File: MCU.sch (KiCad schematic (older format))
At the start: 34 parts, among them Q1 BSS138, SW1 SW_Push, U2 STM32F722RETx

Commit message: Changes made
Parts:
- removed Q1: BSS138, Package_TO_SOT_SMD:SOT-23, symbol Transistor_FET:BSS138
- removed R1: 10k, Resistor_SMD:R_0402_1005Metric, symbol Device:R_Small
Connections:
- net BUZ-_MCU: no longer names the net of U2.24 (PC4)
- net UART6_TX: no longer names the net of U2.37 (PC6)
- no-connect marks 17 -> 19
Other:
- moved on the sheet: C13, C14, FB2
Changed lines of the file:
@@
-$EndComp
-Wire Wire Line
-	5100 2250 5100 2200
-Wire Wire Line
-	5100 2200 5200 2200
-Wire Wire Line
-	5200 2200 5250 2200
-Connection ~ 5200 2200
-Wire Wire Line
-	5200 2150 5200 2200
-Wire Wire Line
-	5200 1900 5450 1900
-Wire Wire Line
-	5200 1900 5200 1950
-Connection ~ 5200 1900
-Wire Wire Line
-	5100 1900 5200 1900
-$Comp
-L Transistor_FET:BSS138 Q1
-U 1 1 6086323C
-P 5450 2100
-F 0 "Q1" V 5699 2100 50  0000 C CNN
-F 1 "BSS138" V 5790 2100 50  0000 C CNN
-F 2 "Package_TO_SOT_SMD:SOT-23" H 5650 2025 50  0001 L CIN
-F 3 "https://www.fairchildsemi.com/datasheets/BS/BSS138.pdf" H 5450 2100 50  0001 L CNN
-	1    5450 2100
-	0    1    1    0
-$EndComp
-$Comp
-L Device:R_Small R1
-U 1 1 60863243
-P 5200 2050
-F 0 "R1" H 5004 2050 50  0000 C CNN
-F 1 "10k" H 5000 1950 50  0000 C CNN
-F 2 "Resistor_SMD:R_0402_1005Metric" H 5200 2050 50  0001 C CNN
-F 3 "~" H 5200 2050 50  0001 C CNN
-	1    5200 2050
-	1    0    0    -1
-$EndComp
-$Comp
-L power:GND #PWR013
-U 1 1 60863249
-P 5100 2250
-F 0 "#PWR013" H 5100 2000 50  0001 C CNN
-F 1 "GND" H 5105 2077 50  0000 C CNN
-F 2 "" H 5100 2250 50  0001 C CNN
-F 3 "" H 5100 2250 50  0001 C CNN
-	1    5100 2250
-	1    0    0    -1
 $EndComp
 Wire Wire Line
@@
 L power:+3.3VA #PWR012
 U 1 1 608633F9
-P 6350 850
-F 0 "#PWR012" H 6350 700 50  0001 C CNN
-F 1 "+3.3VA" H 6365 1023 50  0000 C CNN
-F 2 "" H 6350 850 50  0001 C CNN
-F 3 "" H 6350 850 50  0001 C CNN
-	1    6350 850
+P 5350 1650
+F 0 "#PWR012" H 5350 1500 50  0001 C CNN
+F 1 "+3.3VA" H 5365 1823 50  0000 C CNN
+F 2 "" H 5350 1650 50  0001 C CNN
+F 3 "" H 5350 1650 50  0001 C CNN
+	1    5350 1650
 	1    0    0    -1
 $EndComp
@@
 L Device:C_Small C14
 U 1 1 60863403
-P 6350 950
-F 0 "C14" H 6442 996 50  0000 L CNN
-F 1 "10nF" H 6442 905 50  0000 L CNN
-F 2 "Capacitor_SMD:C_0402_1005Metric" H 6350 950 50  0001 C CNN
-F 3 "~" H 6350 950 50  0001 C CNN
-	1    6350 950
+P 5350 1750
+F 0 "C14" H 5442 1796 50  0000 L CNN
+F 1 "10nF" H 5442 1705 50  0000 L CNN
+F 2 "Capacitor_SMD:C_0402_1005Metric" H 5350 1750 50  0001 C CNN
+F 3 "~" H 5350 1750 50  0001 C CNN
+	1    5350 1750
 	1    0    0    -1
 $EndComp
@@
 L Device:C_Small C13
 U 1 1 60863409
-P 5950 950
-F 0 "C13" H 6042 996 50  0000 L CNN
-F 1 "1uF" H 6042 905 50  0000 L CNN
-F 2 "Capacitor_SMD:C_0402_1005Metric" H 5950 950 50  0001 C CNN
-F 3 "~" H 5950 950 50  0001 C CNN
-	1    5950 950
-	1    0    0    -1
-$EndComp
-Wire Wire Line
-	5400 850  5400 800
-Wire Wire Line
-	5650 850  5400 850
+P 4950 1750
+F 0 "C13" H 5042 1796 50  0000 L CNN
+F 1 "1uF" H 5042 1705 50  0000 L CNN
+F 2 "Capacitor_SMD:C_0402_1005Metric" H 4950 1750 50  0001 C CNN
+F 3 "~" H 4950 1750 50  0001 C CNN
+	1    4950 1750
+	1    0    0    -1
+$EndComp
+Wire Wire Line
+	4400 1650 4400 1600
+Wire Wire Line
+	4650 1650 4400 1650
 $Comp
 L Device:Ferrite_Bead_Small FB2
 U 1 1 60863411
-P 5750 850
-F 0 "FB2" V 5513 850 50  0000 C CNN
-F 1 "100 @ 100 MHz" V 5604 850 50  0000 C CNN
-F 2 "Inductor_SMD:L_0603_1608Metric" V 5680 850 50  0001 C CNN
-F 3 "~" H 5750 850 50  0001 C CNN
-	1    5750 850
+P 4750 1650
+F 0 "FB2" V 4513 1650 50  0000 C CNN
+F 1 "100 @ 100 MHz" V 4604 1650 50  0000 C CNN
+F 2 "Inductor_SMD:L_0603_1608Metric" V 4680 1650 50  0001 C CNN
+F 3 "~" H 4750 1650 50  0001 C CNN
+	1    4750 1650
 	0    1    1    0
 $EndComp
@@
 L power:+3.3V #PWR011
 U 1 1 60863417
-P 5400 800
-F 0 "#PWR011" H 5400 650 50  0001 C CNN
-F 1 "+3.3V" H 5415 973 50  0000 C CNN
-F 2 "" H 5400 800 50  0001 C CNN
-F 3 "" H 5400 800 50  0001 C CNN
-	1    5400 800
+P 4400 1600
+F 0 "#PWR011" H 4400 1450 50  0001 C CNN
+F 1 "+3.3V" H 4415 1773 50  0000 C CNN
+F 2 "" H 4400 1600 50  0001 C CNN
+F 3 "" H 4400 1600 50  0001 C CNN
+	1    4400 1600
 	1    0    0    -1
 $EndComp
@@
 Text HLabel 4000 4150 2    50   Input ~ 0
 M2
-Text HLabel 2700 4750 0    50   Input ~ 0
-UART6_RX
-Text HLabel 2700 4650 0    50   Input ~ 0
-UART6_TX
-Text Label 2700 4550 2    50   ~ 0
-BUZ-_MCU
 Text HLabel 2700 4150 0    50   Input ~ 0
 CURR
@@
 Text Label 2700 2550 2    50   ~ 0
 BOOT0
-Text Label 5100 1900 2    50   ~ 0
-BUZ-_MCU
-Text HLabel 5650 2200 2    50   Input ~ 0
-BUZ-
 Text Label 1350 2900 2    50   ~ 0
 BOOT0
@@
 	2500 2850 2700 2850
 Wire Wire Line
-	5950 1050 6350 1050
+	4950 1850 5350 1850
 $Comp
 L Device:C_Small C8
@@
 L power:GNDA #PWR03
 U 1 1 608B3D37
-P 6350 1050
-F 0 "#PWR03" H 6350 800 50  0001 C CNN
-F 1 "GNDA" H 6355 877 50  0000 C CNN
-F 2 "" H 6350 1050 50  0001 C CNN
-F 3 "" H 6350 1050 50  0001 C CNN
-	1    6350 1050
-	1    0    0    -1
-$EndComp
-Wire Wire Line
-	5850 850  5950 850
-Connection ~ 5950 850
-Wire Wire Line
-	5950 850  6350 850
+P 5350 1850
+F 0 "#PWR03" H 5350 1600 50  0001 C CNN
+F 1 "GNDA" H 5355 1677 50  0000 C CNN
+F 2 "" H 5350 1850 50  0001 C CNN
+F 3 "" H 5350 1850 50  0001 C CNN
+	1    5350 1850
+	1    0    0    -1
+$EndComp
+Wire Wire Line
+	4850 1650 4950 1650
+Connection ~ 4950 1650
+Wire Wire Line
+	4950 1650 5350 1650
 $Comp
 L power:GND #PWR0177
@@
 Wire Wire Line
 	2600 2750 2700 2750
-Connection ~ 6350 850
-Connection ~ 6350 1050
+Connection ~ 5350 1650
+Connection ~ 5350 1850
 $Comp
 L Device:C_Small C11
@@
 NoConn ~ 4000 3250
 NoConn ~ 4000 3350
+NoConn ~ 2700 4650
+NoConn ~ 2700 4550
+Text HLabel 2700 4750 0    50   Input ~ 0
+UART6_RX
 $EndSCHEMATC

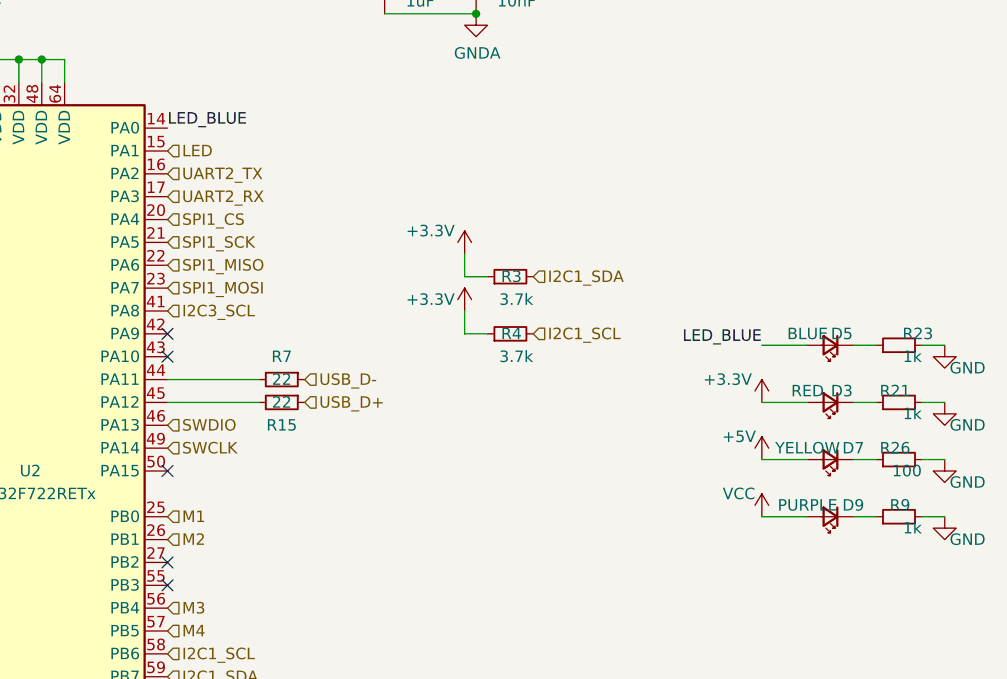
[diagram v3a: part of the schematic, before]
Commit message: Changed some components to match what is in stock
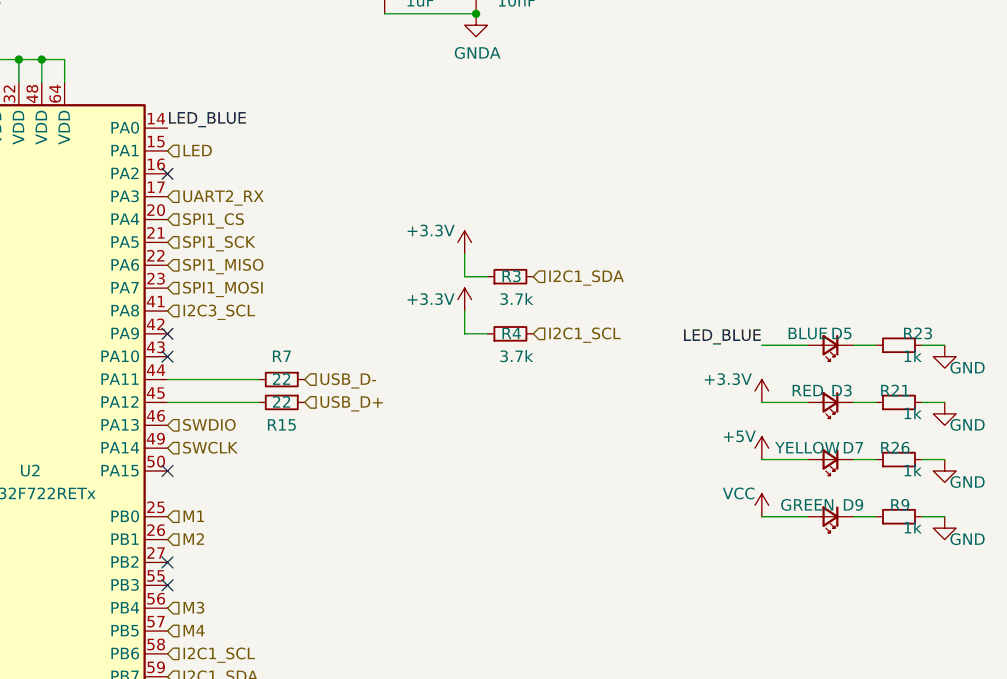
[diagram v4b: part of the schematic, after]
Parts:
- D9: value PURPLE -> GREEN
- R26: value 100 -> 1k
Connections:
- net UART2_TX: no longer names the net of U2.16 (PA2)
- no-connect marks 19 -> 20
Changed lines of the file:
@@
 P 7200 3800
 F 0 "R26" V 7250 3750 50  0000 L CNN
-F 1 "100" V 7150 3700 50  0000 L CNN
+F 1 "1k" V 7150 3700 50  0000 L CNN
 F 2 "Resistor_SMD:R_0402_1005Metric" H 7200 3800 50  0001 C CNN
 F 3 "~" H 7200 3800 50  0001 C CNN
@@
 	1    1550 2800
 	0    -1   -1   0
-$EndComp
-$Comp
-L Switch:SW_Push SW1
-U 1 1 6086331D
-P 1250 2700
-F 0 "SW1" H 1250 2985 50  0000 C CNN
-F 1 "SW_Push" H 1250 2894 50  0000 C CNN
-F 2 "Button_Switch_SMD:SW_SPST_B3U-1000P" H 1250 2900 50  0001 C CNN
-F 3 "~" H 1250 2900 50  0001 C CNN
-	1    1250 2700
-	1    0    0    -1
 $EndComp
 Wire Wire Line
@@
 Text HLabel 4000 3050 2    50   Input ~ 0
 SPI1_MOSI
-Text HLabel 4000 2550 2    50   Input ~ 0
-UART2_TX
 Text HLabel 4000 2650 2    50   Input ~ 0
 UART2_RX
@@
 P 6900 4050
 F 0 "D9" H 6800 4000 50  0000 C CNN
-F 1 "PURPLE" H 7000 4000 50  0000 C CNN
+F 1 "GREEN" H 7000 4000 50  0000 C CNN
 F 2 "LED_SMD:LED_0603_1608Metric" V 6900 4050 50  0001 C CNN
 F 3 "~" V 6900 4050 50  0001 C CNN
@@
 Text HLabel 2700 4750 0    50   Input ~ 0
 UART6_RX
+$Comp
+L Switch:SW_Push SW1
+U 1 1 6086331D
+P 1250 2700
+F 0 "SW1" H 1250 2985 50  0000 C CNN
+F 1 "SW_Push" H 1250 2894 50  0000 C CNN
+F 2 "Button_Switch_SMD:SW_SPST_B3U-1000P" H 1250 2900 50  0001 C CNN
+F 3 "~" H 1250 2900 50  0001 C CNN
+	1    1250 2700
+	1    0    0    -1
+$EndComp
+NoConn ~ 4000 2550
 $EndSCHEMATC
